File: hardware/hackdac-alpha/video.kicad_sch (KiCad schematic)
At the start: 84 parts, among them J1 VIDEO OUT, U1 AD768, U2 MAX4104, U3 TLE2082, U4 MAX4104

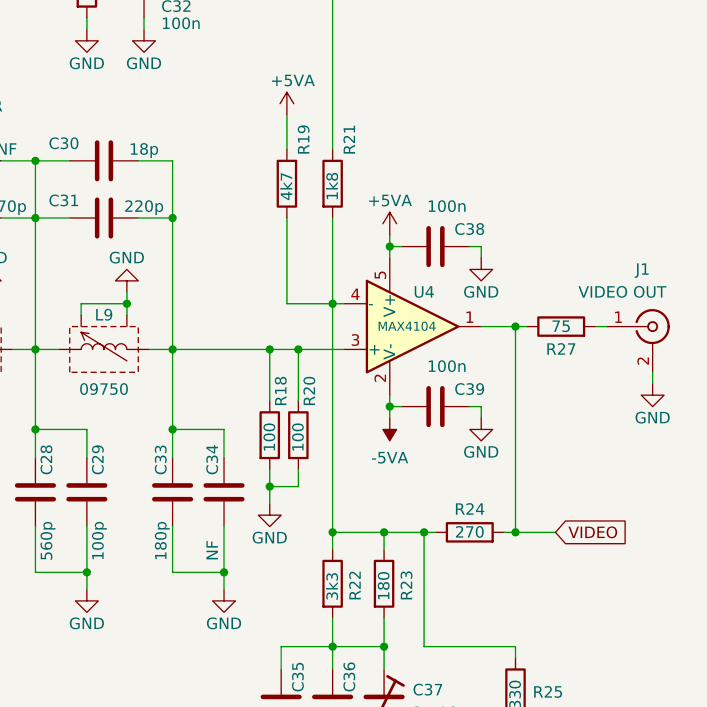
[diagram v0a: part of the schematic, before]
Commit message: Update component values
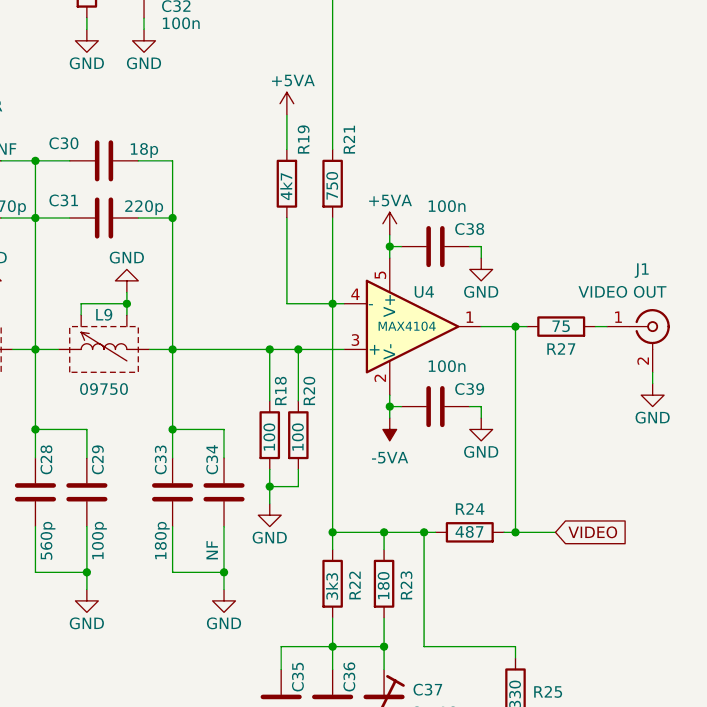
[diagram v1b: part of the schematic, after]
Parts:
- R21: value 1k8 -> 750
- R24: value 270 -> 487
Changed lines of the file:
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@@
 			)
 		)
-		(property "Value" "1k8"
+		(property "Value" "750"
 			(at 243.205 70.485 90)
 			(effects
@@
 			)
 		)
-		(property "Value" "270"
+		(property "Value" "487"
 			(at 258.445 107.315 90)
 			(effects

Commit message: Update with V2 mods
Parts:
- R21: value 750 -> 470
- R24: value 487 -> 330
- R25: value 330 -> 220
- R26: value 100 -> 75
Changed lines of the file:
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@@
 			)
 		)
-		(property "Value" "750"
+		(property "Value" "470"
 			(at 243.205 70.485 90)
 			(effects
@@
 			)
 		)
-		(property "Value" "100"
-			(at 263.525 141.605 90)
+		(property "Value" "75"
+			(at 263.525 140.97 90)
 			(effects
 				(font
@@
 			)
 		)
-		(property "Value" "487"
+		(property "Value" "330"
 			(at 258.445 107.315 90)
 			(effects
@@
 			)
 		)
-		(property "Value" "330"
+		(property "Value" "220"
 			(at 263.525 127 90)
 			(effects

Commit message: Beginnings of V3 - re-evalulate filter
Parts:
- C10: value 1n -> 1n5
- C11: value 560p -> NF
- C12, C17, C18, C29: value 100p -> NF
- C13: value 82p -> NF
- C14: value 100p -> 270p
- C15: value 680p -> 3n9
- C16: value 2n2 -> NF
- C19: value 100p -> 300p
- C20: value 1n -> NF
- C21: value 220p -> NF
- C22: value 82p -> 300p
- C24, C40: value 390p -> NF
- C25: value 220p -> 620p
- C26: value NF -> 270p
- C27: value 270p -> NF
- C28: value 560p -> 680p
- C30: value 18p -> NF
- C31: value 220p -> 240p
- C36: value 47p -> 68pF
- C41: value 560p -> 1n
- R13, R20: value 100 -> NF
- R14, R18: value 100 -> 50
- R22: value 3k3 -> NF
- R23: value 180 -> 169
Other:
- moved on the sheet: C10, C11, C15, C16, C21, C22, C24, C25, C26, C27, C40, C41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

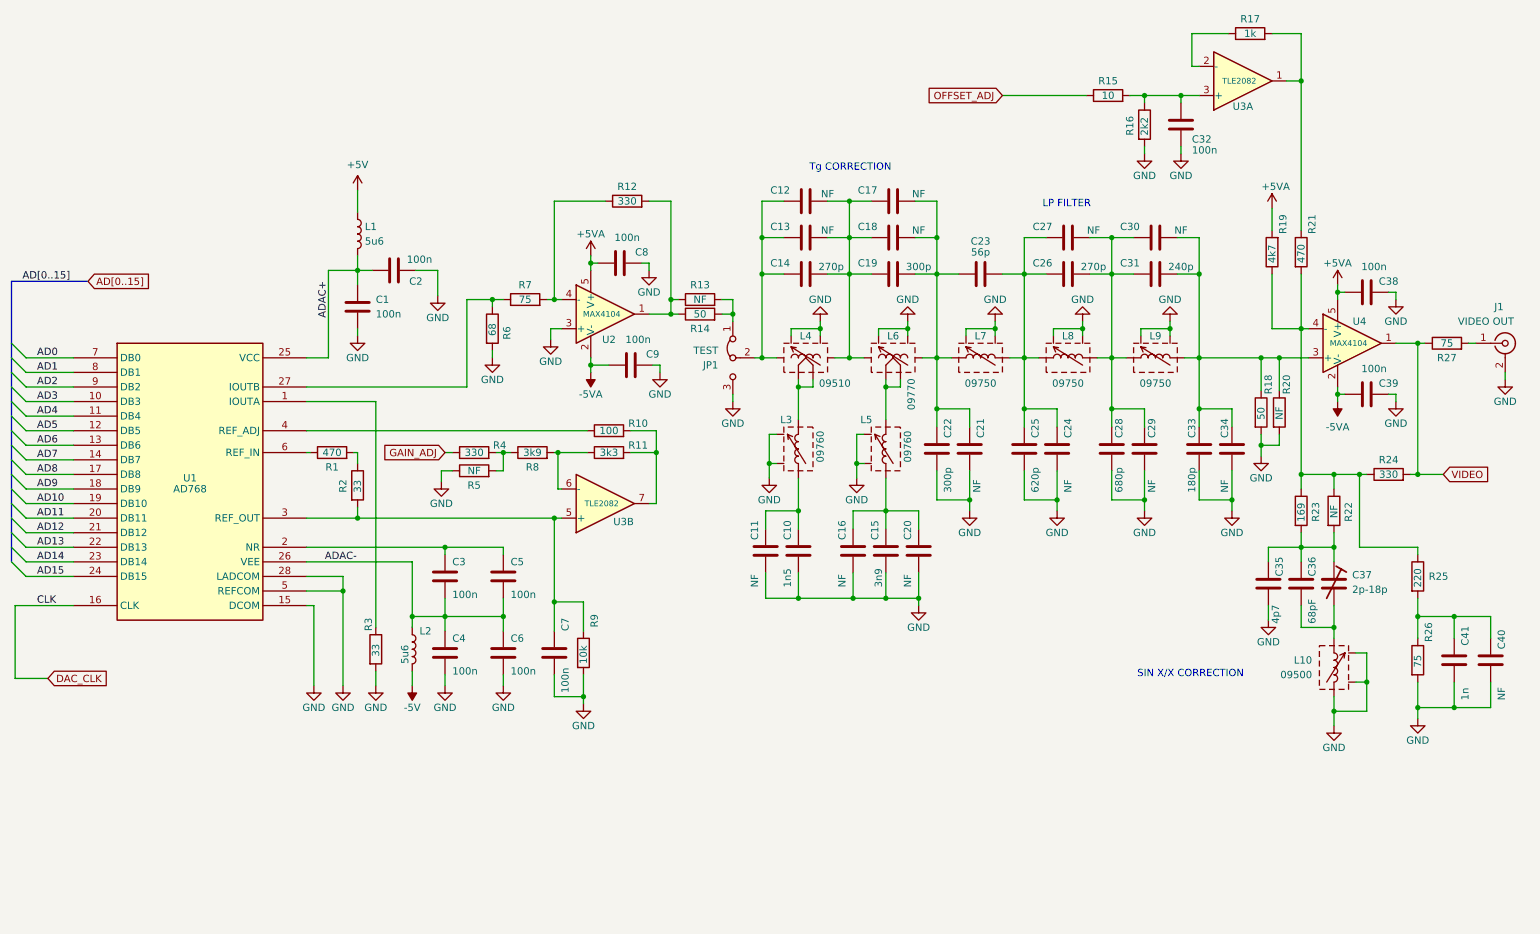
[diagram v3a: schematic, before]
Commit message: More V3 component rationalisation
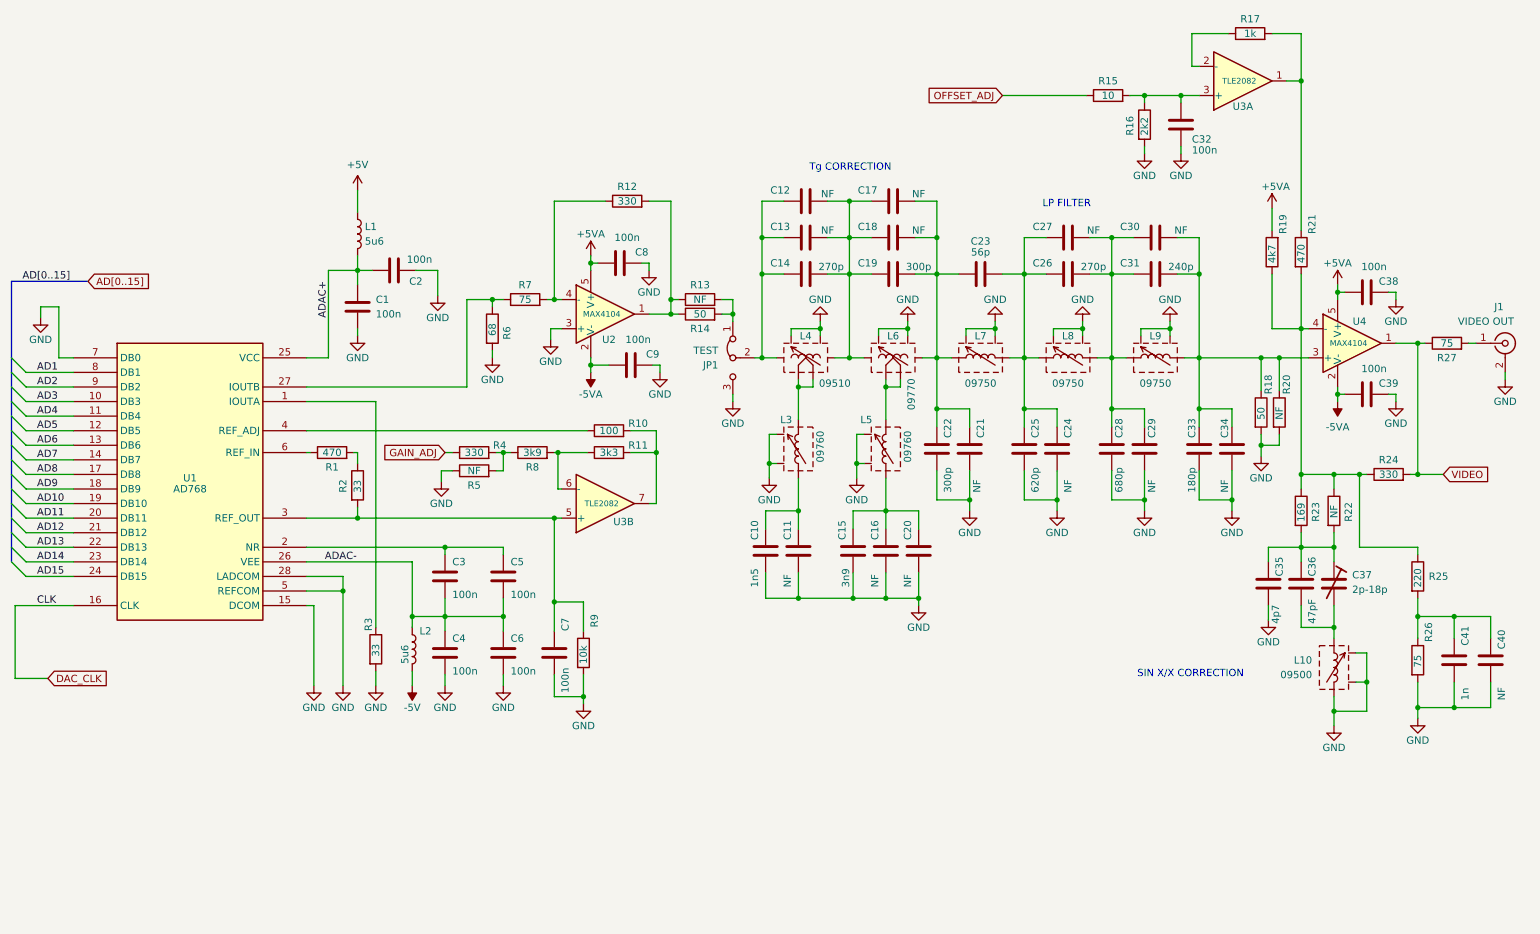
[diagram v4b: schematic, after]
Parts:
- C36: value 68pF -> 47pF
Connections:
- net AD0 is gone; now on net GND: U1.7 (DB0)
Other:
- moved on the sheet: C10, C11, C15, C16

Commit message: V3 PCB WIP
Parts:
- renumbered C22 to C21, C21 to C22, C25 to C24, C24 to C25, C27 to C26, C26 to C27, C41 to C40, C40 to C41, R23 to R22, R22 to R23

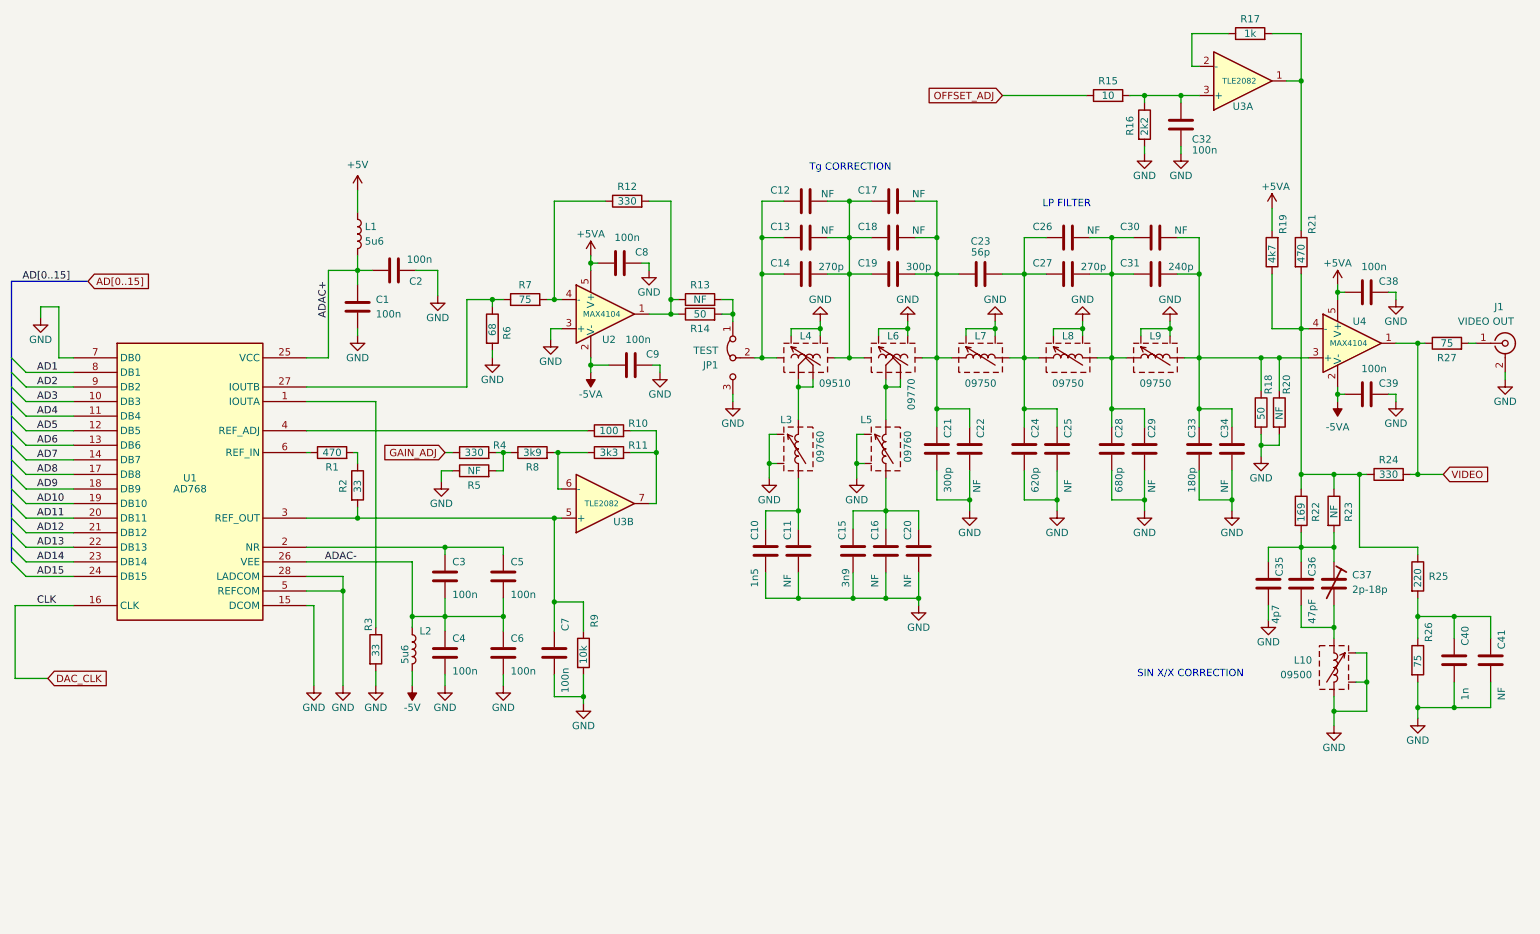
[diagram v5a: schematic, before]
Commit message: Optional caps for DAC supply
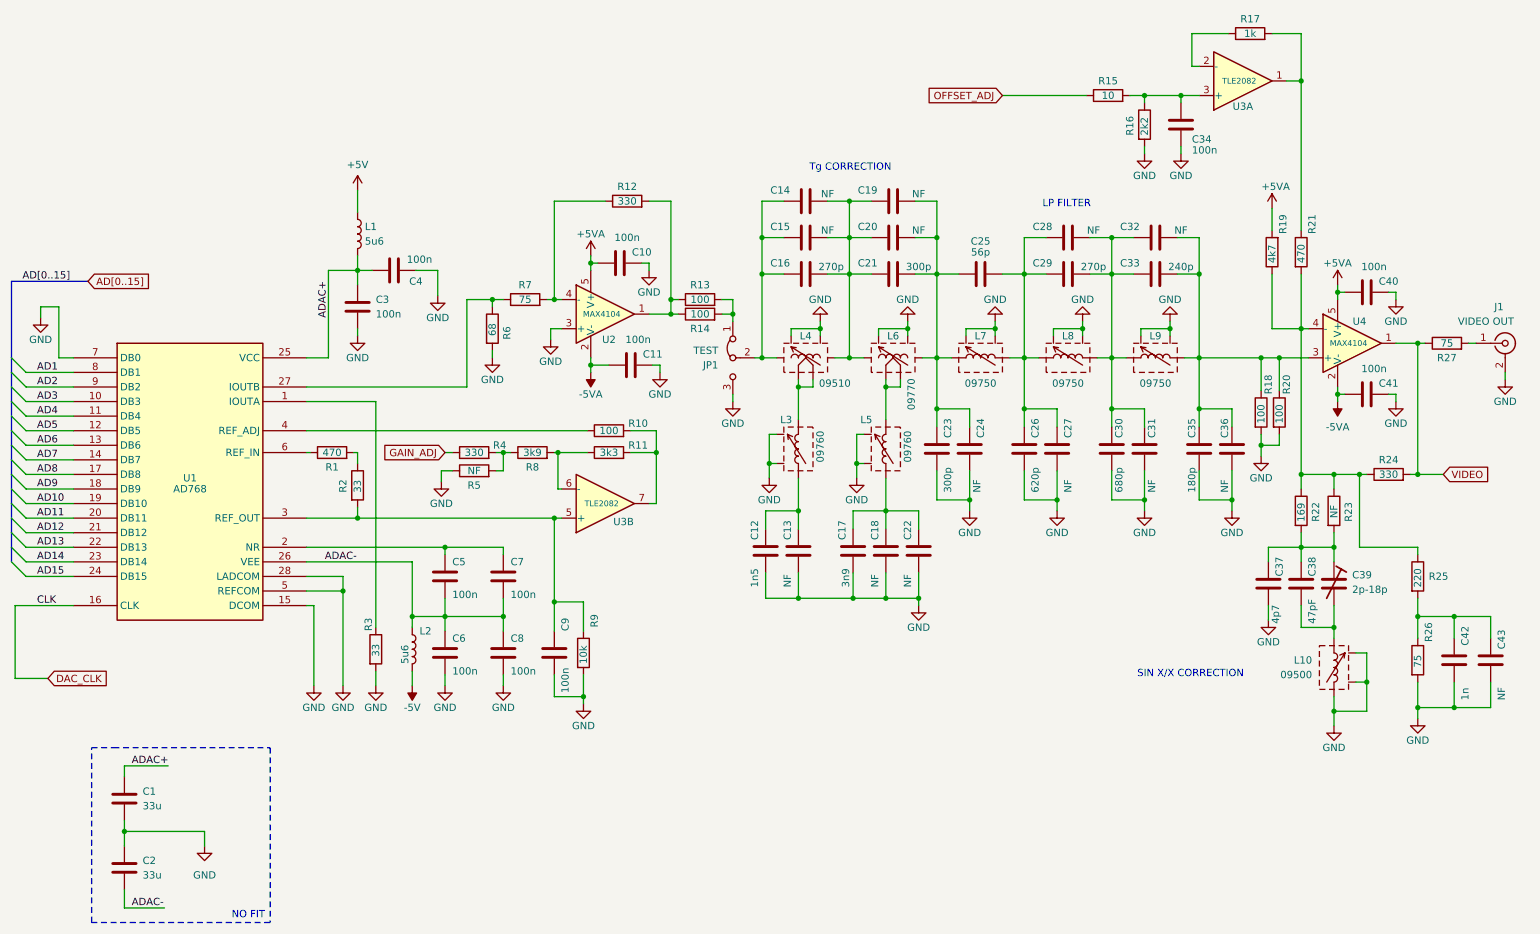
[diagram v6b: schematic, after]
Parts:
- added C1, C2: 33u, Capacitor_SMD:C_1210_3225Metric, symbol Device:C
- R13, R20: value NF -> 100
- R14, R18: value 50 -> 100
- renumbered C8 to C10, C9 to C11, C10 to C12, C11 to C13, C12 to C14, C13 to C15, C14 to C16, C15 to C17, C16 to C18, C17 to C19, C18 to C20, C19 to C21, C20 to C22, C21 to C23, C22 to C24, C23 to C25, C24 to C26, C25 to C27, C26 to C28, C27 to C29, C1 to C3, C28 to C30, C29 to C31, C30 to C32, C31 to C33, C32 to C34, C33 to C35, C34 to C36, C35 to C37, C36 to C38, C37 to C39, C2 to C4, C38 to C40, C39 to C41, C40 to C42, C41 to C43, C3 to C5, C4 to C6, C5 to C7, C6 to C8, C7 to C9
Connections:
- net ADAC+: now also C1.1
- net ADAC-: now also C2.2
- net GND: now also C1.2, C2.1
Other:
- note added: "NO FIT"

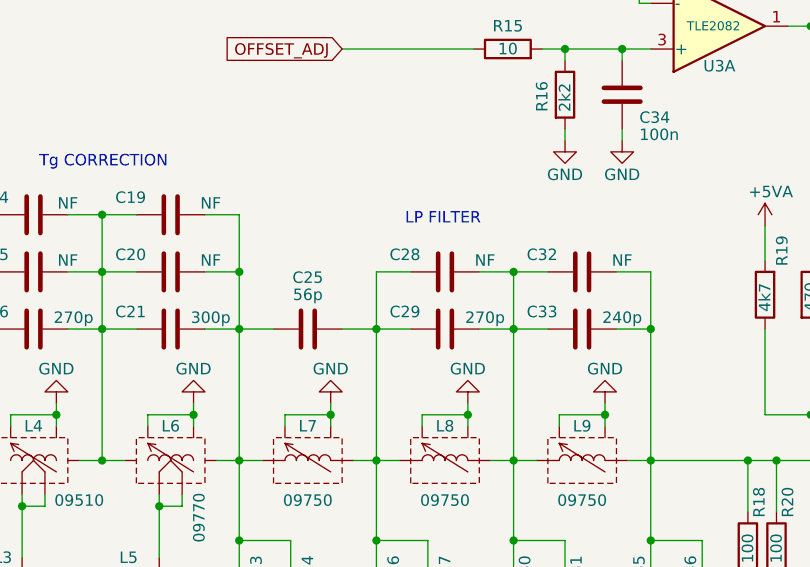
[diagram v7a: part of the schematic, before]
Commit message: Fixed a couple of incorrect component values
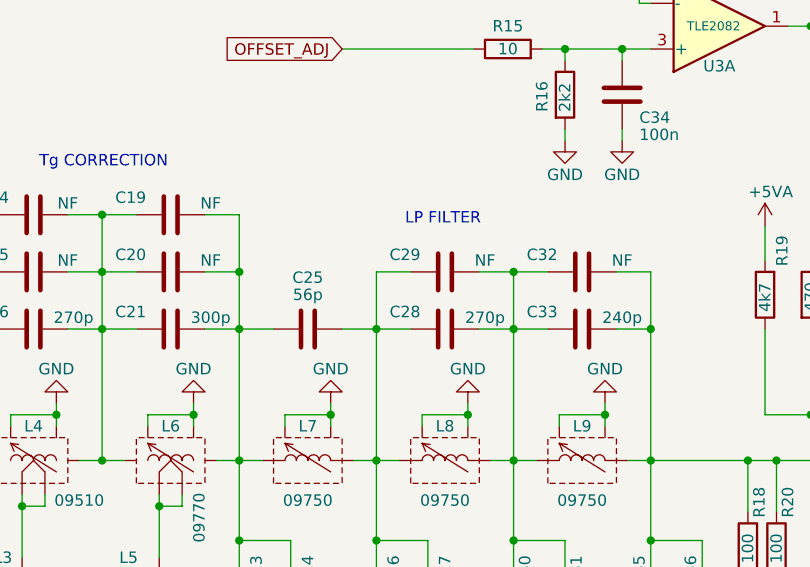
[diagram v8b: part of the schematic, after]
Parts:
- C28: value NF -> 270p
- C29: value 270p -> NF
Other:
- moved on the sheet: C28, C29
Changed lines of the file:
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@@
 	(symbol
 		(lib_id "Device:C")
-		(at 202.565 66.04 90)
+		(at 202.565 72.39 90)
 		(unit 1)
 		(exclude_from_sim no)
@@
 		(dnp no)
 		(property "Reference" "C28"
-			(at 198.12 64.135 90)
-			(effects
-				(font
-					(size 1.27 1.27)
-				)
-			)
-		)
-		(property "Value" "NF"
-			(at 207.01 64.77 90)
+			(at 198.12 70.485 90)
+			(effects
+				(font
+					(size 1.27 1.27)
+				)
+			)
+		)
+		(property "Value" "270p"
+			(at 207.01 71.12 90)
 			(effects
 				(font
@@
 		)
 		(property "Footprint" "Capacitor_SMD:C_0603_1608Metric"
-			(at 206.375 65.0748 0)
+			(at 206.375 71.4248 0)
 			(effects
 				(font
@@
 		)
 		(property "Datasheet" "~"
-			(at 202.565 66.04 0)
-			(effects
-				(font
-					(size 1.27 1.27)
-				)
-				(hide yes)
-			)
-		)
-		(property "Description" ""
-			(at 202.565 66.04 0)
+			(at 202.565 72.39 0)
+			(effects
+				(font
+					(size 1.27 1.27)
+				)
+				(hide yes)
+			)
+		)
+		(property "Description" ""
+			(at 202.565 72.39 0)
 			(effects
 				(font
@@
 	(symbol
 		(lib_id "Device:C")
-		(at 202.565 72.39 90)
+		(at 202.565 66.04 90)
 		(unit 1)
 		(exclude_from_sim no)
@@
 		(dnp no)
 		(property "Reference" "C29"
-			(at 198.12 70.485 90)
-			(effects
-				(font
-					(size 1.27 1.27)
-				)
-			)
-		)
-		(property "Value" "270p"
-			(at 207.01 71.12 90)
+			(at 198.12 64.135 90)
+			(effects
+				(font
+					(size 1.27 1.27)
+				)
+			)
+		)
+		(property "Value" "NF"
+			(at 207.01 64.77 90)
 			(effects
 				(font
@@
 		)
 		(property "Footprint" "Capacitor_SMD:C_0603_1608Metric"
-			(at 206.375 71.4248 0)
+			(at 206.375 65.0748 0)
 			(effects
 				(font
@@
 		)
 		(property "Datasheet" "~"
-			(at 202.565 72.39 0)
-			(effects
-				(font
-					(size 1.27 1.27)
-				)
-				(hide yes)
-			)
-		)
-		(property "Description" ""
-			(at 202.565 72.39 0)
-			(effects
-				(font
+			(at 202.565 66.04 0)
+			(effects
+				(font
+					(size 1.27 1.27)
+				)
+				(hide yes)
+			)
+		)
+		(property "Description" ""
+			(at 202.565 66.04 0)
+			(effects
+				(font
